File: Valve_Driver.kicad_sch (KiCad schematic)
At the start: 7 parts, among them U5 TC1508S

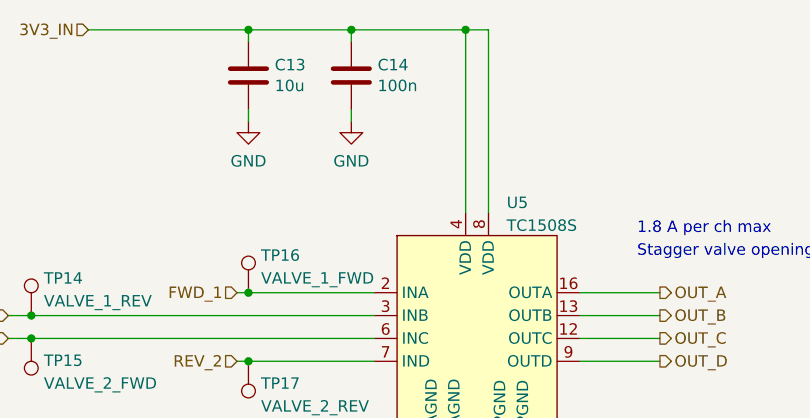
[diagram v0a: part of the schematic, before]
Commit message: Add 5V boost converter and begin redesign of PCB
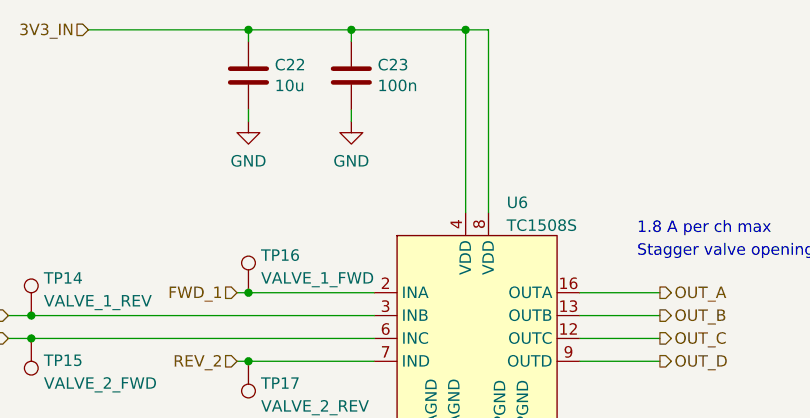
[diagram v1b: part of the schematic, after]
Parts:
- renumbered C13 to C22, C14 to C23, U5 to U6
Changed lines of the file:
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@@
   (symbol (lib_id "Device:C") (at 132.08 72.39 0) (unit 1)
     (in_bom yes) (on_board yes)
-    (property "Reference" "C13" (id 0) (at 135.001 71.2216 0)
+    (property "Reference" "C22" (id 0) (at 135.001 71.2216 0)
       (effects (font (size 1.27 1.27)) (justify left))
     )
@@
   (symbol (lib_id "co2_sensor_node:TC1508S") (at 157.48 90.17 0) (unit 1)
     (in_bom yes) (on_board yes) (fields_autoplaced)
-    (property "Reference" "U5" (id 0) (at 160.7694 86.521 0)
+    (property "Reference" "U6" (id 0) (at 160.7694 86.521 0)
       (effects (font (size 1.27 1.27)) (justify left))
     )
@@
   (symbol (lib_id "power:GND") (at 143.51 77.47 0) (unit 1)
     (in_bom yes) (on_board yes) (fields_autoplaced)
-    (property "Reference" "#PWR050" (id 0) (at 143.51 83.82 0)
+    (property "Reference" "#PWR063" (id 0) (at 143.51 83.82 0)
       (effects (font (size 1.27 1.27)) hide)
     )
@@
   (symbol (lib_id "power:GND") (at 157.48 119.38 0) (unit 1)
     (in_bom yes) (on_board yes) (fields_autoplaced)
-    (property "Reference" "#PWR051" (id 0) (at 157.48 125.73 0)
+    (property "Reference" "#PWR064" (id 0) (at 157.48 125.73 0)
       (effects (font (size 1.27 1.27)) hide)
     )
@@
   (symbol (lib_id "power:GND") (at 132.08 77.47 0) (unit 1)
     (in_bom yes) (on_board yes) (fields_autoplaced)
-    (property "Reference" "#PWR049" (id 0) (at 132.08 83.82 0)
+    (property "Reference" "#PWR062" (id 0) (at 132.08 83.82 0)
       (effects (font (size 1.27 1.27)) hide)
     )
@@
   (symbol (lib_id "Device:C") (at 143.51 72.39 0) (unit 1)
     (in_bom yes) (on_board yes)
-    (property "Reference" "C14" (id 0) (at 146.431 71.2216 0)
+    (property "Reference" "C23" (id 0) (at 146.431 71.2216 0)
       (effects (font (size 1.27 1.27)) (justify left))
     )

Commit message: More layout work
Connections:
- net 3V3_IN renamed +5V
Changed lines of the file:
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@@
   (junction (at 132.08 104.14) (diameter 0) (color 0 0 0 0)
   )
+  (junction (at 132.08 67.31) (diameter 0) (color 0 0 0 0)
+  )
   (junction (at 143.51 67.31) (diameter 0) (color 0 0 0 0)
   )
-  (junction (at 132.08 67.31) (diameter 0) (color 0 0 0 0)
-  )
   (junction (at 107.95 99.06) (diameter 0) (color 0 0 0 0)
   )
@@
     (stroke (width 0) (type default) (color 0 0 0 0))
   )
+  (wire (pts (xy 132.08 66.04) (xy 132.08 67.31))
+    (stroke (width 0) (type default) (color 0 0 0 0))
+  )
   (wire (pts (xy 154.94 114.3) (xy 154.94 116.84))
     (stroke (width 0) (type default) (color 0 0 0 0))
@@
   )
   (wire (pts (xy 160.02 114.3) (xy 160.02 116.84))
-    (stroke (width 0) (type default) (color 0 0 0 0))
-  )
-  (wire (pts (xy 114.3 67.31) (xy 132.08 67.31))
     (stroke (width 0) (type default) (color 0 0 0 0))
   )
@@
   (hierarchical_label "OUT_B" (shape output) (at 177.8 99.06 0)
     (effects (font (size 1.27 1.27)) (justify left))
-  )
-  (hierarchical_label "3V3_IN" (shape input) (at 114.3 67.31 180)
-    (effects (font (size 1.27 1.27)) (justify right))
   )
   (symbol (lib_id "Connector:TestPoint") (at 132.08 96.52 0) (unit 1)
@@
       (effects (font (size 1.27 1.27)) hide)
     )
+    (pin "1")
+  )
+  (symbol (lib_id "power:+5V") (at 132.08 66.04 0) (unit 1)
+    (in_bom yes) (on_board yes) (fields_autoplaced)
+    (property "Reference" "#PWR?" (id 0) (at 132.08 69.85 0)
+      (effects (font (size 1.27 1.27)) hide)
+    )
+    (property "Value" "+5V" (id 1) (at 132.08 62.4642 0))
+    (property "Footprint" "" (id 2) (at 132.08 66.04 0)
+      (effects (font (size 1.27 1.27)) hide)
+    )
+    (property "Datasheet" "" (id 3) (at 132.08 66.04 0)
+      (effects (font (size 1.27 1.27)) hide)
+    )

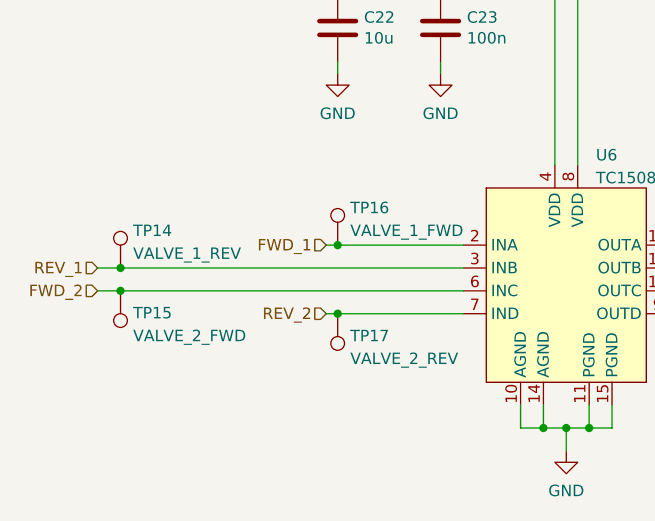
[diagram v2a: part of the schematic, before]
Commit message: Finish component placement
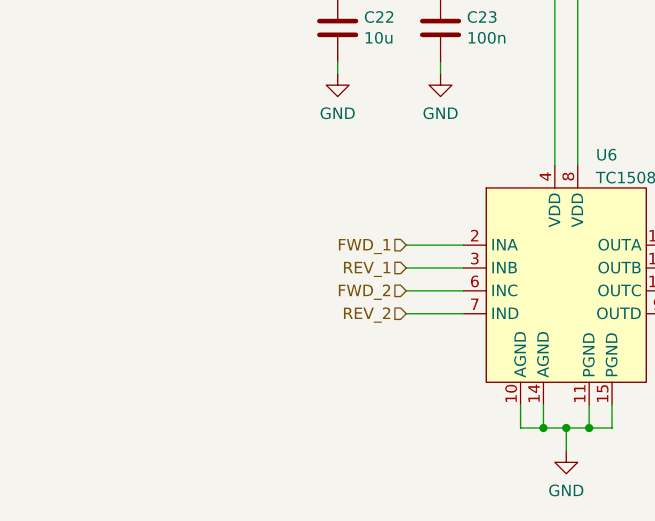
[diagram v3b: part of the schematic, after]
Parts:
- removed TP14: VALVE_1_REV, TestPoint:TestPoint_Loop_D2.50mm_Drill1.0mm_LowProfile, symbol Connector:TestPoint
- removed TP15: VALVE_2_FWD, TestPoint:TestPoint_Loop_D2.50mm_Drill1.0mm_LowProfile, symbol Connector:TestPoint
- removed TP16: VALVE_1_FWD, TestPoint:TestPoint_Loop_D2.50mm_Drill1.0mm_LowProfile, symbol Connector:TestPoint
- removed TP17: VALVE_2_REV, TestPoint:TestPoint_Loop_D2.50mm_Drill1.0mm_LowProfile, symbol Connector:TestPoint
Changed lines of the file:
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@@
     (rev "2")
   )
-  (junction (at 132.08 96.52) (diameter 0) (color 0 0 0 0)
-  )
   (junction (at 157.48 116.84) (diameter 0) (color 0 0 0 0)
   )
-  (junction (at 107.95 101.6) (diameter 0) (color 0 0 0 0)
-  )
   (junction (at 160.02 116.84) (diameter 0) (color 0 0 0 0)
   )
-  (junction (at 132.08 104.14) (diameter 0) (color 0 0 0 0)
-  )
   (junction (at 132.08 67.31) (diameter 0) (color 0 0 0 0)
   )
   (junction (at 143.51 67.31) (diameter 0) (color 0 0 0 0)
   )
-  (junction (at 107.95 99.06) (diameter 0) (color 0 0 0 0)
-  )
   (junction (at 156.21 67.31) (diameter 0) (color 0 0 0 0)
   )
   (junction (at 154.94 116.84) (diameter 0) (color 0 0 0 0)
   )
-  (wire (pts (xy 130.81 104.14) (xy 132.08 104.14))
-    (stroke (width 0) (type default) (color 0 0 0 0))
-  )
   (wire (pts (xy 156.21 67.31) (xy 158.75 67.31))
     (stroke (width 0) (type default) (color 0 0 0 0))
@@
     (stroke (width 0) (type default) (color 0 0 0 0))
   )
-  (wire (pts (xy 132.08 96.52) (xy 146.05 96.52))
+  (wire (pts (xy 139.7 96.52) (xy 146.05 96.52))
     (stroke (width 0) (type default) (color 0 0 0 0))
   )
@@
     (stroke (width 0) (type default) (color 0 0 0 0))
   )
-  (wire (pts (xy 132.08 104.14) (xy 146.05 104.14))
+  (wire (pts (xy 139.7 104.14) (xy 146.05 104.14))
     (stroke (width 0) (type default) (color 0 0 0 0))
   )
@@
     (stroke (width 0) (type default) (color 0 0 0 0))
   )
-  (wire (pts (xy 105.41 101.6) (xy 107.95 101.6))
-    (stroke (width 0) (type default) (color 0 0 0 0))
-  )
   (wire (pts (xy 143.51 68.58) (xy 143.51 67.31))
     (stroke (width 0) (type default) (color 0 0 0 0))
   )
-  (wire (pts (xy 130.81 96.52) (xy 132.08 96.52))
-    (stroke (width 0) (type default) (color 0 0 0 0))
-  )
   (wire (pts (xy 168.91 101.6) (xy 177.8 101.6))
     (stroke (width 0) (type default) (color 0 0 0 0))
@@
     (stroke (width 0) (type default) (color 0 0 0 0))
   )
-  (wire (pts (xy 107.95 101.6) (xy 146.05 101.6))
+  (wire (pts (xy 139.7 101.6) (xy 146.05 101.6))
     (stroke (width 0) (type default) (color 0 0 0 0))
   )
@@
     (stroke (width 0) (type default) (color 0 0 0 0))
   )
-  (wire (pts (xy 107.95 99.06) (xy 146.05 99.06))
+  (wire (pts (xy 139.7 99.06) (xy 146.05 99.06))
     (stroke (width 0) (type default) (color 0 0 0 0))
   )
   (wire (pts (xy 156.21 67.31) (xy 156.21 87.63))
-    (stroke (width 0) (type default) (color 0 0 0 0))
-  )
-  (wire (pts (xy 105.41 99.06) (xy 107.95 99.06))
     (stroke (width 0) (type default) (color 0 0 0 0))
   )
@@
     (effects (font (size 1.27 1.27)) (justify left bottom))
   )
-  (hierarchical_label "FWD_2" (shape input) (at 105.41 101.6 180)
+  (hierarchical_label "FWD_2" (shape input) (at 139.7 101.6 180)
     (effects (font (size 1.27 1.27)) (justify right))
   )
@@
     (effects (font (size 1.27 1.27)) (justify left))
   )
-  (hierarchical_label "FWD_1" (shape input) (at 130.81 96.52 180)
+  (hierarchical_label "FWD_1" (shape input) (at 139.7 96.52 180)
     (effects (font (size 1.27 1.27)) (justify right))
   )
@@
     (effects (font (size 1.27 1.27)) (justify left))
   )
-  (hierarchical_label "REV_2" (shape input) (at 130.81 104.14 180)
-    (effects (font (size 1.27 1.27)) (justify right))
-  )
-  (hierarchical_label "REV_1" (shape input) (at 105.41 99.06 180)
+  (hierarchical_label "REV_2" (shape input) (at 139.7 104.14 180)
+    (effects (font (size 1.27 1.27)) (justify right))
+  )
+  (hierarchical_label "REV_1" (shape input) (at 139.7 99.06 180)
     (effects (font (size 1.27 1.27)) (justify right))
   )
   (hierarchical_label "OUT_B" (shape output) (at 177.8 99.06 0)
     (effects (font (size 1.27 1.27)) (justify left))
-  )
-  (symbol (lib_id "Connector:TestPoint") (at 132.08 96.52 0) (unit 1)
-    (in_bom yes) (on_board yes) (fields_autoplaced)
-    (property "Reference" "TP16" (id 0) (at 133.477 92.3833 0)
-      (effects (font (size 1.27 1.27)) (justify left))
-    )
-    (property "Value" "VALVE_1_FWD" (id 1) (at 133.477 94.9202 0)
-      (effects (font (size 1.27 1.27)) (justify left))
-    )
-    (property "Footprint" "TestPoint:TestPoint_Loop_D2.50mm_Drill1.0mm_LowProfile" (id 2) (at 137.16 96.52 0)
-      (effects (font (size 1.27 1.27)) hide)
-    )
-    (property "Datasheet" "~" (id 3) (at 137.16 96.52 0)
-      (effects (font (size 1.27 1.27)) hide)
-    )
-    (pin "1")
-  )
-  (symbol (lib_id "Connector:TestPoint") (at 107.95 99.06 0) (unit 1)
-    (in_bom yes) (on_board yes) (fields_autoplaced)
-    (property "Reference" "TP14" (id 0) (at 109.347 94.9233 0)
-      (effects (font (size 1.27 1.27)) (justify left))
-    )
-    (property "Value" "VALVE_1_REV" (id 1) (at 109.347 97.4602 0)
-      (effects (font (size 1.27 1.27)) (justify left))
-    )
-    (property "Footprint" "TestPoint:TestPoint_Loop_D2.50mm_Drill1.0mm_LowProfile" (id 2) (at 113.03 99.06 0)
-      (effects (font (size 1.27 1.27)) hide)
-    )
-    (property "Datasheet" "~" (id 3) (at 113.03 99.06 0)
-      (effects (font (size 1.27 1.27)) hide)
-    )
-    (pin "1")
   )
   (symbol (lib_id "Device:C") (at 132.08 72.39 0) (unit 1)
@@
     (pin "1")
     (pin "2")
-  )
-  (symbol (lib_id "Connector:TestPoint") (at 132.08 104.14 180) (unit 1)
-    (in_bom yes) (on_board yes) (fields_autoplaced)
-    (property "Reference" "TP17" (id 0) (at 133.477 106.6073 0)
-      (effects (font (size 1.27 1.27)) (justify right))
-    )
-    (property "Value" "VALVE_2_REV" (id 1) (at 133.477 109.1442 0)
-      (effects (font (size 1.27 1.27)) (justify right))
-    )
-    (property "Footprint" "TestPoint:TestPoint_Loop_D2.50mm_Drill1.0mm_LowProfile" (id 2) (at 127 104.14 0)
-      (effects (font (size 1.27 1.27)) hide)
-    )
-    (property "Datasheet" "~" (id 3) (at 127 104.14 0)
-      (effects (font (size 1.27 1.27)) hide)
-    )
-    (pin "1")
   )
   (symbol (lib_id "co2_sensor_node:TC1508S") (at 157.48 90.17 0) (unit 1)
@@
   (symbol (lib_id "power:+5V") (at 132.08 66.04 0) (unit 1)
     (in_bom yes) (on_board yes) (fields_autoplaced)
-    (property "Reference" "#PWR?" (id 0) (at 132.08 69.85 0)
+    (property "Reference" "#PWR0102" (id 0) (at 132.08 69.85 0)
       (effects (font (size 1.27 1.27)) hide)
     )
@@
       (effects (font (size 1.27 1.27)) hide)
     )
-    (pin "1")
-  )
-  (symbol (lib_id "Connector:TestPoint") (at 107.95 101.6 180) (unit 1)
-    (in_bom yes) (on_board yes) (fields_autoplaced)
-    (property "Reference" "TP15" (id 0) (at 109.347 104.0673 0)
-      (effects (font (size 1.27 1.27)) (justify right))
-    )
-    (property "Value" "VALVE_2_FWD" (id 1) (at 109.347 106.6042 0)
-      (effects (font (size 1.27 1.27)) (justify right))
-    )
-    (property "Footprint" "TestPoint:TestPoint_Loop_D2.50mm_Drill1.0mm_LowProfile" (id 2) (at 102.87 101.6 0)
-      (effects (font (size 1.27 1.27)) hide)
-    )
-    (property "Datasheet" "~" (id 3) (at 102.87 101.6 0)
-      (effects (font (size 1.27 1.27)) hide)
-    )
